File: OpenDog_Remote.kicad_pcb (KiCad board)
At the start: 2 copper layers, 81 x 51 mm, 37 parts, among them J1 Conn_01x03_Pin, J10 Conn_01x03_Pin, J11 Conn_01x03_Pin, J12 Conn_01x02_Pin, J13 Conn_01x03_Pin, J14 Conn_01x03_Pin, J15 Conn_01x03_Pin, J16 Conn_01x03_Pin, J17 NRF, J18 Conn_02x08_Odd_Even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

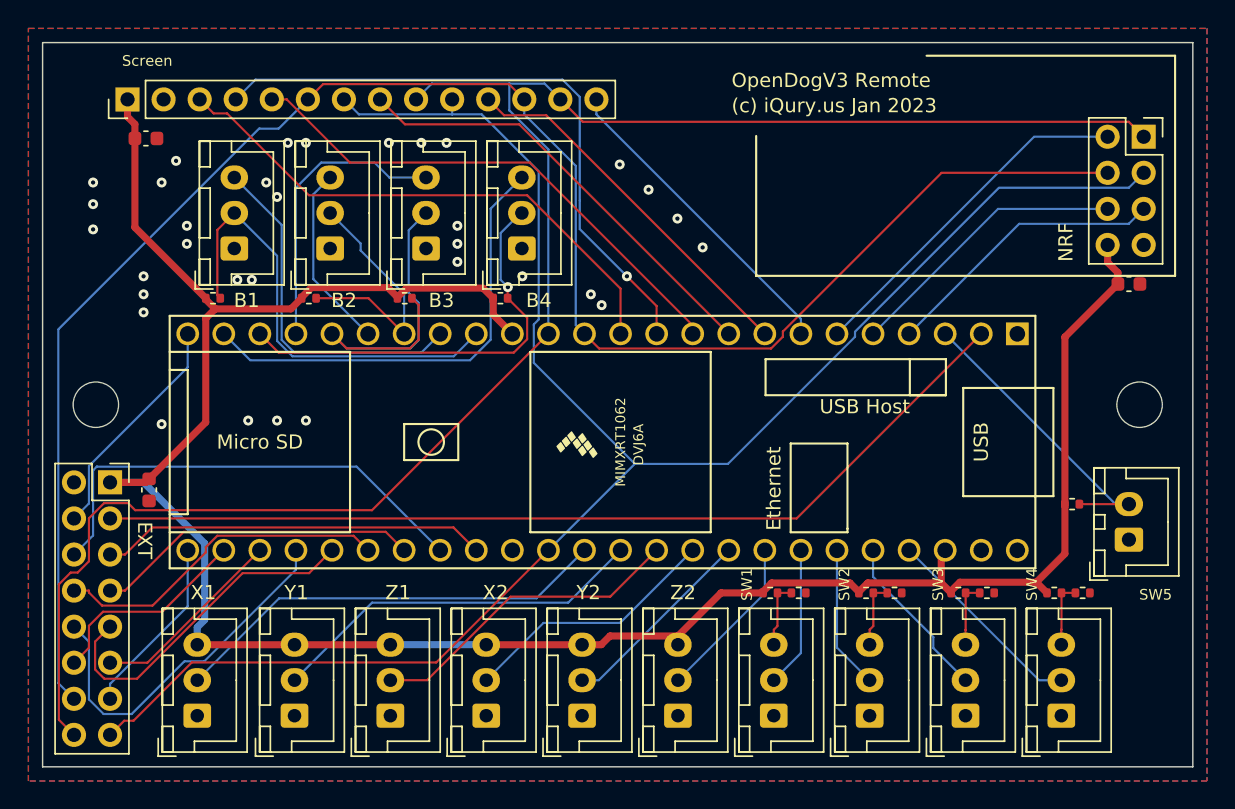
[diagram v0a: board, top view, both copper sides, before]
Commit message: Added JLCPCB part #, round some board corners.
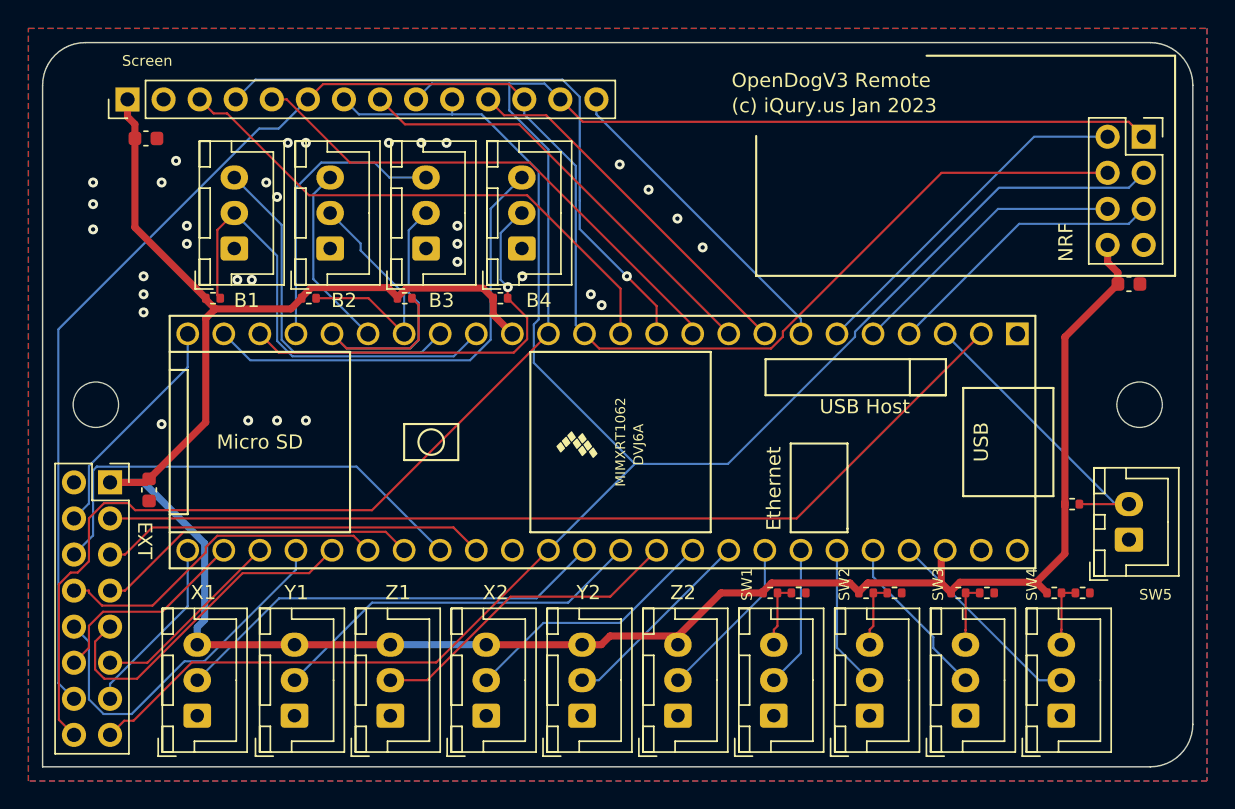
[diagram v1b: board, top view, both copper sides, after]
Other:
- outline, holes or cut-outs redrawn
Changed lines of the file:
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@@
   (gr_line (start 139.75 66.425) (end 139.75 50.925)
     (stroke (width 0.15) (type default)) (layer "F.SilkS"))
-  (gr_line (start 60 101) (end 60 50)
+  (gr_line (start 60 101) (end 60 53)
     (stroke (width 0.1) (type default)) (layer "Edge.Cuts"))
-  (gr_line (start 60 50) (end 141 50)
+  (gr_line (start 63 50) (end 138 50)
     (stroke (width 0.1) (type default)) (layer "Edge.Cuts"))
-  (gr_line (start 141 101) (end 60 101)
+  (gr_line (start 138 101) (end 60 101)
     (stroke (width 0.1) (type default)) (layer "Edge.Cuts"))
-  (gr_line (start 141 50) (end 141 101)
+  (gr_line (start 141 53) (end 141 98)
+    (stroke (width 0.1) (type default)) (layer "Edge.Cuts"))
+  (gr_arc (start 141 98) (mid 140.12132 100.12132) (end 138 101)
+    (stroke (width 0.1) (type default)) (layer "Edge.Cuts"))
+  (gr_arc (start 60 53) (mid 60.87868 50.87868) (end 63 50)
+    (stroke (width 0.1) (type default)) (layer "Edge.Cuts"))
+  (gr_arc (start 138 50) (mid 140.12132 50.87868) (end 141 53)
     (stroke (width 0.1) (type default)) (layer "Edge.Cuts"))
   (gr_text "~{TFT_CS}" (at 71.938 55.534 90) (layer "B.SilkS")
